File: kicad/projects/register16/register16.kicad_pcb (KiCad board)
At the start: 2 copper layers, 203.2 x 97.8 mm, 42 parts, among them J1 INPUT_ENABLE, J10 LOW, J2 OUTPUT_ENABLE, J3 CONTENTS, J4 Control_signal_backplane, J5 Aux_connection, J6 Bus_connection, J7 HIGH, J8 LOW, J9 HIGH, U1 74HCT04, U2 74HCT377, U3 74HCT377, U4 74HCT245, U5 74HCT245, U6 74HCT245, U7 74HCT245

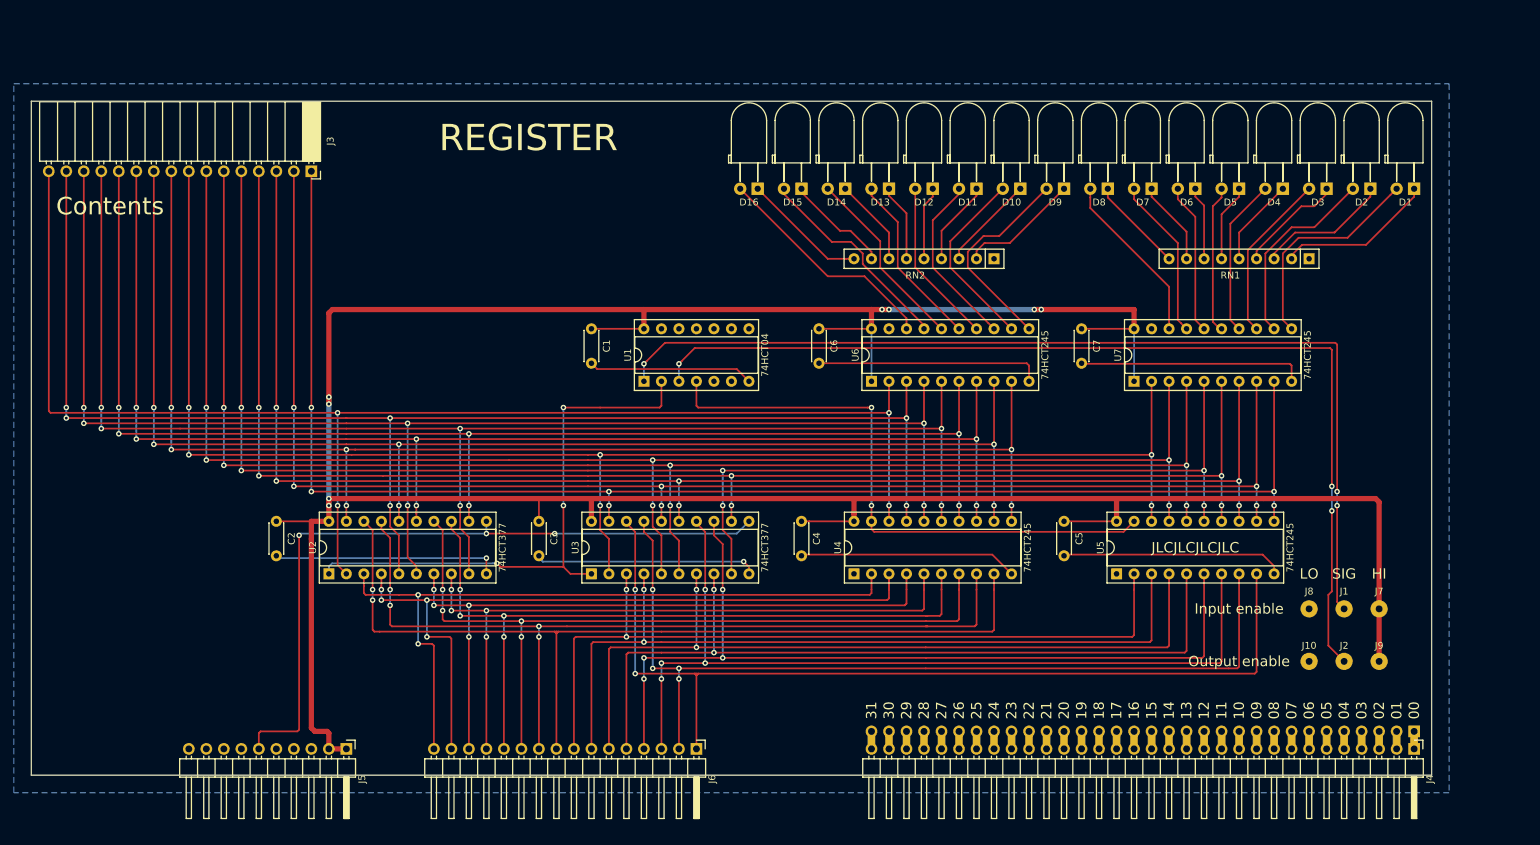
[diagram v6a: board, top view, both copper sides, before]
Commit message: Add aux and bus footprints. Tidy up in register. Add power cap to reg.
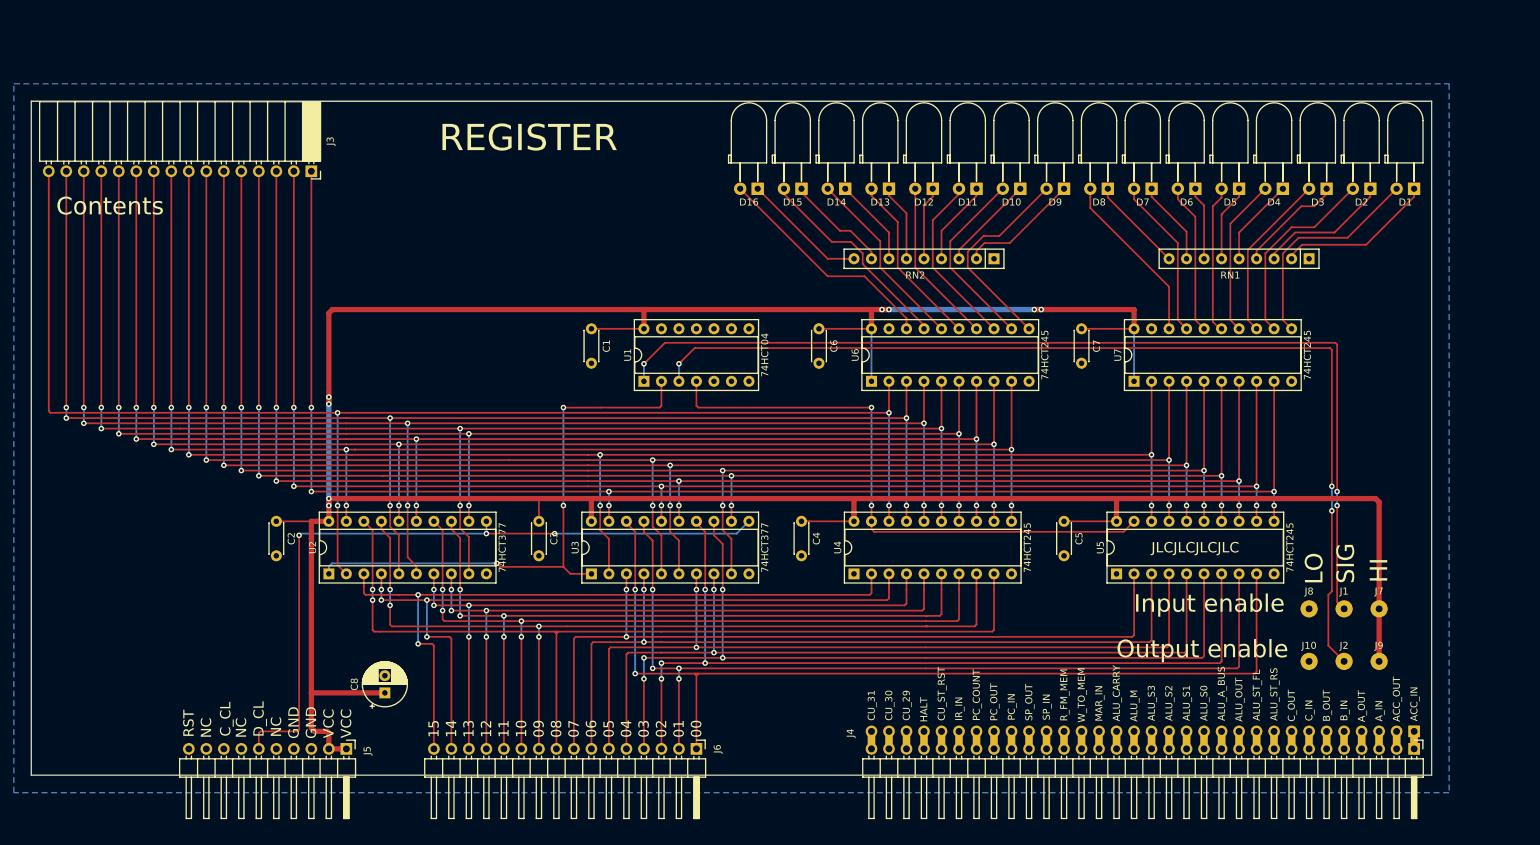
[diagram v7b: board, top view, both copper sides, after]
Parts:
- added C8: 330uF, Capacitor_THT:CP_Radial_D6.3mm_P2.50mm, F.Cu at (125.0, 124.0)
- C2, C3, C4, C5, C6, C7: value C -> 0.1.uF
- J4: footprint eight-bit-computer:backplane-connector -> eight-bit-computer:backplane-connector-annotated
- J5: footprint Connector_PinHeader_2.54mm:PinHeader_1x10_P2.54mm_Horizontal -> eight-bit-computer:aux-connection
- J6: footprint Connector_PinHeader_2.54mm:PinHeader_1x16_P2.54mm_Horizontal -> eight-bit-computer:bus-connection
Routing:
- net GND: track 218.9 -> 0.00 mm, vias 2 -> 0
- net VCC: track 447.3 -> 457.9 mm

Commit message: Rounded edges, spaced vias in power, shorteded LEDs.
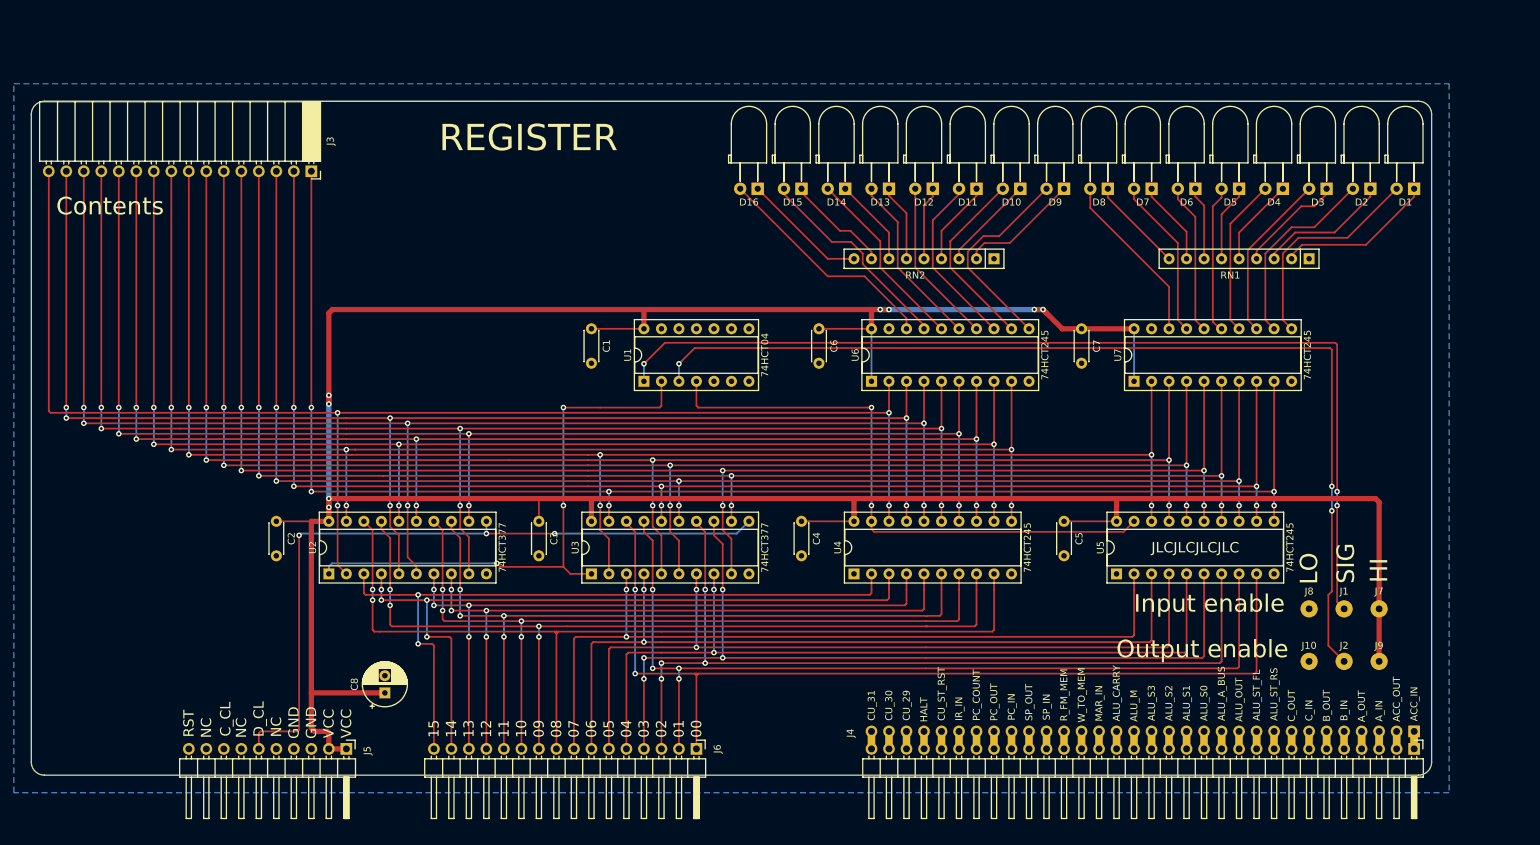
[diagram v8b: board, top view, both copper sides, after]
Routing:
- net Net-(J4-Pad9): track 0.00 -> 2.54 mm
- net Net-(J4-Pad8): track 0.00 -> 2.54 mm
- net Net-(J4-Pad7): track 0.00 -> 2.54 mm
- net Net-(J4-Pad6): track 0.00 -> 2.54 mm
- net Net-(J4-Pad5): track 0.00 -> 2.54 mm
- net Net-(J4-Pad4): track 0.00 -> 2.54 mm
- net Net-(J4-Pad32): track 0.00 -> 2.54 mm
- net Net-(J4-Pad31): track 0.00 -> 2.54 mm
- net Net-(J4-Pad30): track 0.00 -> 2.54 mm
- net Net-(J4-Pad3): track 0.00 -> 2.54 mm
- net Net-(J4-Pad29): track 0.00 -> 2.54 mm
- net Net-(J4-Pad28): track 0.00 -> 2.54 mm
- net Net-(J4-Pad27): track 0.00 -> 2.54 mm
- net Net-(J4-Pad26): track 0.00 -> 2.54 mm
- net Net-(J4-Pad25): track 0.00 -> 2.54 mm
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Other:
- outline, holes or cut-outs redrawn
